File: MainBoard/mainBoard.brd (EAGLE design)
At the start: 99.3 x 99.3 mm, 89 parts, among them IC1 74HC238, IC2 74HC238, IC3 74HC151D, J1 22-05-7038-03, J2 22-05-7038-03, J3 22-05-7038-03, J4 22-05-7038-03, J5 22-05-7038-03, J6 22-05-7038-03, J7 22-05-7038-03, J8 22-05-7038-03, Q1 BC847ASMD, Q10 BC847ASMD, Q2 BC847ASMD, Q5 BC847ASMD, Q6 BC847ASMD, Q9 BC847ASMD, X1 PWR12, X2 MSTBA2, X3 MSTBA2, X4 MSTBA2, X5 MSTBA2, X6 MSTBA2, X7 MSTBA2

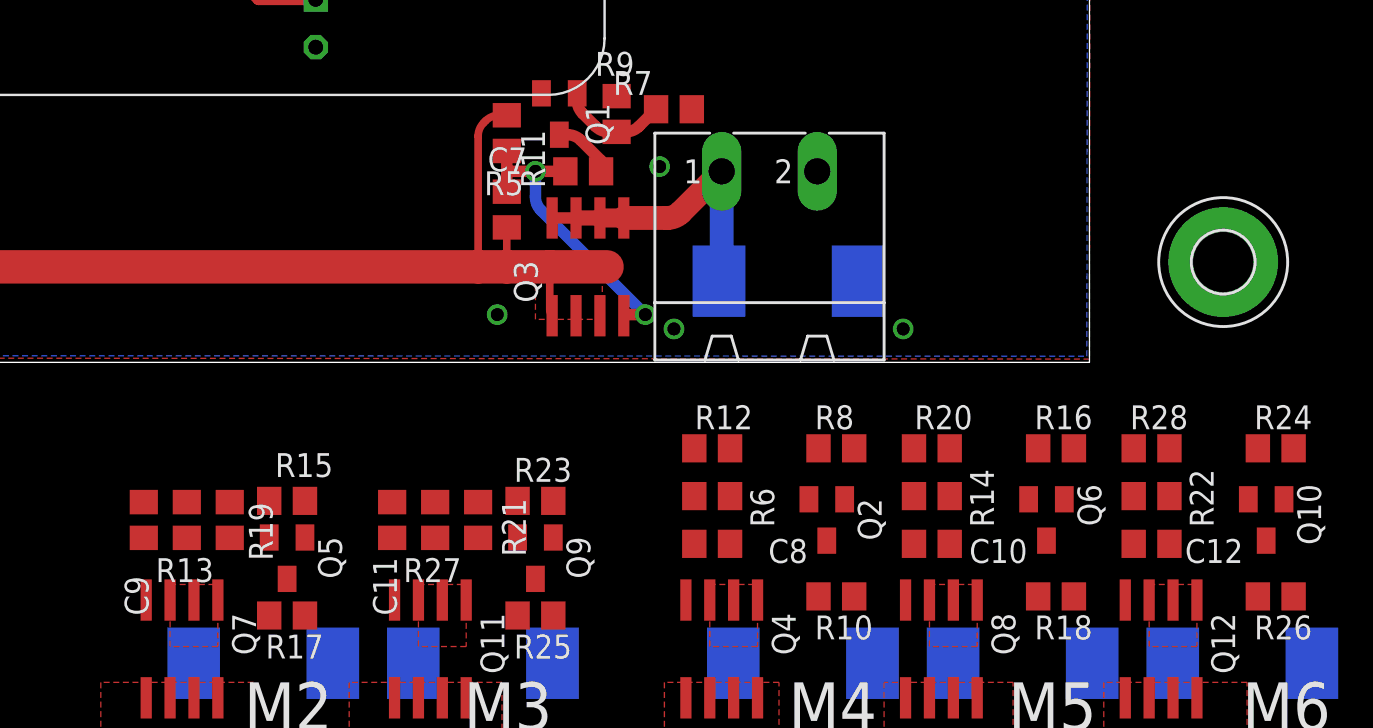
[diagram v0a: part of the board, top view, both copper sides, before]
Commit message: mainboard updates motor curcuit
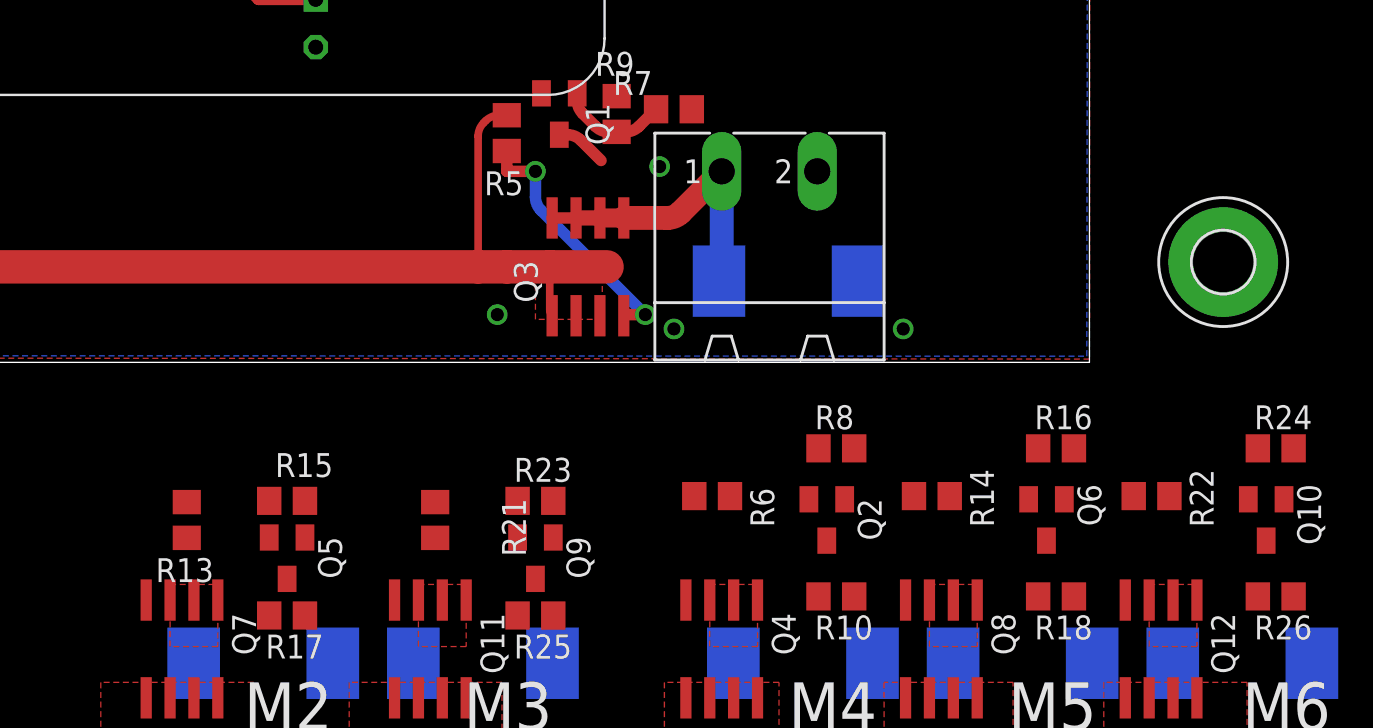
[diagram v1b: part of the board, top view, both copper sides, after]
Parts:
- removed C10, C11, C12, C7, C8, C9: 100n, rcl:C0805
- removed R11, R12, R19, R20, R27, R28: 560, rcl:R0805
- R15, R16, R23, R24, R7, R8: value 10k -> 100
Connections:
- removed net N$10: Q9.3, R27.1
- removed net N$14: Q2.3, R12.1
- removed net N$16: C10.2, Q8.4, R14.1, R20.2
- removed net N$19: C12.2, Q12.4, R22.1, R28.2
- removed net N$4: Q1.3, R11.1
- removed net N$6: Q5.3, R19.1
- net +15V: no longer C10.1, C11.1, C12.1, C7.1, C8.1, C9.1
- net N$13: now also Q2.3; no longer C8.2, R12.2
- net N$17: now also Q8.4, R14.1; no longer R20.1
- net N$2: now also Q5.3; no longer C9.2, R19.2
- net N$21: now also Q12.4, R22.1; no longer R28.1
- net N$3: now also Q1.3; no longer C7.2, R11.2
- net N$8: now also Q9.3; no longer C11.2, R27.2
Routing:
- net N$4: track 3.30 -> 0.00 mm
- net +15V: track 173.4 -> 171.3 mm

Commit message: mainboard updates
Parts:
- removed D5, D7: (no value), diode:SMC
- removed Q10, Q6: BC847ASMD, transistor-npn:SOT23
- removed Q12, Q8: (no value), transistor-power:SO-08
- removed R14, R22: 1k2, rcl:R0805
- removed R16, R24: 100, rcl:R0805
- removed R18, R26: 18k, rcl:R0805
- removed X6, X7: MSTBA2, con-phoenix-508:MSTBA2
- moved Q2 72.9 mm to (14.7, 9.91)
- moved R10 70.5 mm to (17.8, 5.84), turned to 90 degrees
- moved R8 69.6 mm to (17.8, 10.2), turned to 270 degrees
- moved X5 68.2 mm to (25.4, 5.08)
- moved R6 66.5 mm to (14.0, 5.33), flipped to the bottom, turned to 270 degrees
- moved Q4 65.7 mm to (18.0, 7.37), flipped to the bottom, turned to 0 degrees
- moved D3 61.5 mm to (26.4, 5.33)
- moved Q9 41.4 mm to (33.8, 9.91)
- moved X4 39.9 mm to (44.5, 5.08)
- moved R25 38.2 mm to (36.8, 5.84), turned to 90 degrees
- moved R23 37.4 mm to (36.8, 10.2), turned to 270 degrees
- moved Q11 35.4 mm to (37.1, 7.37), flipped to the bottom, turned to 0 degrees
- moved R21 34.4 mm to (33.0, 5.33), flipped to the bottom
- moved X3 33.8 mm to (63.5, 5.08)
- moved D6 30.4 mm to (45.5, 5.33)
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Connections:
- removed net N$17: Q6.3, Q8.4, R14.1
- removed net N$18: Q6.1, R16.2, R18.2
- removed net N$21: Q10.3, Q12.4, R22.1
- removed net N$22: Q10.1, R24.2, R26.2
- removed net WP5: D5.C, Q8.5, Q8.6, Q8.7, Q8.8, X6.1
- removed net WP5C: IC1.12, R16.1
- removed net WP6: D7.C, Q12.5, Q12.6, Q12.7, Q12.8, X7.1
- removed net WP6C: IC1.10, R24.1
- net +15V: no longer Q12.1, Q12.2, Q12.3, Q8.1, Q8.2, Q8.3, R14.2, R22.2
- net GND: no longer D5.A, D7.A, Q10.2, Q6.2, R18.1, R26.1, X6.2, X7.2
- net WP4C: now also IC1.12; no longer IC1.11
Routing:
- net WP4C: track 0.00 -> 75.3 mm
- net WP3C: track 0.00 -> 57.8 mm
- net WP2C: track 0.00 -> 40.4 mm
- net WP1C: track 0.00 -> 22.9 mm
- net +15V: track 171.3 -> 188.5 mm
- net WP1: track 15.9 -> 0.00 mm
- net N$3: track 16.5 -> 6.89 mm, vias 2 -> 1
- net N$8: track 0.00 -> 6.89 mm, vias 0 -> 1
- net N$13: track 0.00 -> 6.89 mm, vias 0 -> 1
- net N$2: track 0.00 -> 6.89 mm, vias 0 -> 1
- net N$15: track 0.00 -> 5.62 mm
- net N$11: track 0.00 -> 5.62 mm
- net N$7: track 0.00 -> 5.58 mm
- added copper zone on layer 16, net +15V
- added copper zone on layer 16, net WP1
- added copper zone on layer 16, net WP2
- added copper zone on layer 16, net WP3
- added copper zone on layer 16, net WP4
- removed copper zone on layer 1, net +15V
- removed copper zone on layer 1, net WP2
- removed copper zone on layer 1, net WP3
- removed copper zone on layer 1, net WP4
- removed copper zone on layer 1, net WP5
- removed copper zone on layer 1, net WP6
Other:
- outline, holes or cut-outs redrawn
- board text removed: "GND [+]"
- board text removed: "M2"
- board text removed: "M3"
- board text removed: "M4"
- board text removed: "M5"
- board text removed: "M6"

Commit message: mainboard updates
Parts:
- removed J6, J7, J8: 22-05-7038-03, con-molex:7395-03
- added D5: (no value), diode:DO-214AC
- added Q6: BC847ASMD, transistor-npn:SOT23
- added Q8: (no value), transistor-power:SO-08
- added R11: 100, rcl:R0805
- added R12: 18k, rcl:R0805
- added R14: 1k2, rcl:R0805
- added X6: MSTBA2, con-phoenix-508:MSTBA2
- D2, D3, D4, D6: device diode:SMC -> diode:DO-214AC
- moved D6 51.3 mm to (94.0, 22.1), turned to 90 degrees
- moved D3 37.1 mm to (63.5, 5.59)
- moved R4 33.6 mm to (111.3, 31.2)
- moved D4 20.1 mm to (44.5, 5.59)
- moved IC3 12.4 mm to (83.6, 55.9), turned to 90 degrees
- moved IC2 12.2 mm to (83.6, 68.3)
- moved J1 8.39 mm to (94.0, 77.5)
- moved J2 8.39 mm to (94.0, 69.3)
- moved J3 8.39 mm to (94.0, 61.2)
- moved J4 8.39 mm to (94.0, 53.1)
- moved J5 8.39 mm to (94.0, 45.0)
- moved IC1 2.84 mm to (85.6, 32.8)
- moved U$2 2.54 mm to (35.3, 75.9)
- moved D2 1.05 mm to (82.5, 5.59)
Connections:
- removed net S6_3V: IC2.10, J6.1
- removed net S6_DAT: IC3.14, J6.2
- removed net S7_3V: IC2.9, J7.1
- removed net S7_DAT: IC3.13, J7.2
- removed net S8_3V: IC2.7, J8.1
- removed net S8_DAT: IC3.12, J8.2
- new net N$4: Q6.3, Q8.4, R14.1
- new net N$6: Q6.1, R11.2, R12.2
- new net WP5: D6.C, Q8.5, Q8.6, Q8.7, Q8.8, X6.1
- new net WP5C: IC1.11, R11.1
- net +15V: now also Q8.1, Q8.2, Q8.3, R14.2
- net GND: now also D5.A, Q6.2, R12.1, X6.2; no longer J6.3, J7.3, J8.3
- net WP2: now also D3.C; no longer D4.C
- net WP3: now also D4.C; no longer D6.C
- net WP4: now also D5.C; no longer D3.C
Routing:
- net +15V: track 188.5 -> 208.3 mm
- net N$4: track 0.00 -> 15.9 mm, vias 0 -> 1
- net WP5C: track 0.00 -> 13.1 mm, vias 0 -> 2
- net N$6: track 0.00 -> 11.1 mm
- net WP4C: track 75.3 -> 78.8 mm
- net WP3C: track 57.8 -> 61.0 mm
- net WP2C: track 40.4 -> 43.2 mm
- net WP1C: track 22.9 -> 25.5 mm
- net +5V: track 127.0 -> 125.6 mm
- net SPI1_MOSI: track 18.6 -> 19.8 mm
- net SPI1_SCK: track 25.1 -> 26.2 mm
- net LED_ERR: track 34.0 -> 35.0 mm
- net SPI1_MISO: track 11.7 -> 12.7 mm
- net STM_TXD: track 48.5 -> 47.4 mm
- net STM_RXD: track 54.0 -> 53.0 mm
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- added copper zone on layer 16, net WP5
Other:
- board text removed: "1"
- board text removed: "2"
- board text removed: "3"
- board text removed: "4"
- board text removed: "7"
- board text removed: "8"
- board text removed: "S6"
- board text removed: "S7"
- board text removed: "S8"

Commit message: mainboard updates
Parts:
- IC1, IC2: value 74HC238 -> 74HC138D
- moved R4 60.5 mm to (62.0, 66.3), turned to 0 degrees
- moved IC3 2.87 mm to (81.5, 53.8)
- moved IC2 2.27 mm to (81.5, 67.3)
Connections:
- removed net 3V3: U$2.1, U$2.23
- removed net N$24: IC2.4, IC2.5
- removed net VCC: IC1.16
- new net +3V3: IC1.16, IC2.16, IC3.16, U$2.1, U$2.23
- net +5V: no longer IC2.16, IC3.16
- net FREQ: now also U$2.28
- net GND: now also IC2.4, IC2.5
- net SEN_A0: now also U$2.27
- net SEN_A1: now also U$2.26
- net SEN_A2: now also U$2.25
- net SEN_ENABLE: now also U$2.17
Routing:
- net +3V3: track 0.00 -> 145.3 mm, vias 0 -> 3
- net 3V3: track 48.0 -> 0.00 mm, vias 2 -> 0
- net SEN_A0: track 0.00 -> 47.4 mm
- net SEN_ENABLE: track 0.00 -> 43.8 mm, vias 0 -> 2
- net SEN_A2: track 0.00 -> 41.7 mm
- net SEN_A1: track 0.00 -> 40.7 mm
- net FREQ: track 0.00 -> 38.0 mm
- net S1_DAT: track 0.00 -> 30.3 mm
- net S2_DAT: track 0.00 -> 23.5 mm
- net S5_3V: track 0.00 -> 23.0 mm, vias 0 -> 1
- net S5_DAT: track 0.00 -> 18.7 mm, vias 0 -> 1
- net S4_3V: track 0.00 -> 16.7 mm, vias 0 -> 1
- net S3_DAT: track 0.00 -> 16.5 mm
- net S1_3V: track 0.00 -> 14.9 mm
- net S3_3V: track 0.00 -> 11.4 mm, vias 0 -> 1
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
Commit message: board updates
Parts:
- added SJ1, SJ2: (no value), jumper:SJ_2
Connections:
- new net RPI_3V3: PCB1.1, PCB1.17, SJ1.1
- new net RPI_5V: PCB1.2, PCB1.4, SJ2.1
- new net STM_3V3: SJ1.3, U$2.1, U$2.23, U$2.40
- new net STM_5V: SJ2.3, U$2.3
- net +3V3: now also SJ1.2; no longer U$2.1, U$2.23
- net +5V: now also SJ2.2; no longer PCB1.2, PCB1.4, U$2.3
- net GND: now also U$2.10, U$2.11, U$2.12, U$2.13, U$2.16, U$2.18, U$2.19, U$2.20, U$2.32, U$2.33, U$2.34, U$2.5, U$2.6, U$2.7, U$2.8, U$2.9
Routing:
- net +3V3: track 145.3 -> 84.8 mm
- net STM_3V3: track 0.00 -> 51.2 mm
- net +5V: track 125.8 -> 77.6 mm, vias 3 -> 1
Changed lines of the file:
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@@
 <?xml version="1.0" encoding="utf-8"?>
 <!DOCTYPE eagle SYSTEM "eagle.dtd">
-<eagle version="6.5.0">
+<eagle version="6.6.0">
 <drawing>
 <settings>
@@
 <attribute name="NAME" x="86.614" y="16.002" size="1.778" layer="25" ratio="10" rot="R90"/>
 </element>
+<element name="SJ1" library="jumper" package="SJ_2" value="" x="-10.668" y="-3.048"/>
+<element name="SJ2" library="jumper" package="SJ_2" value="" x="-10.668" y="-7.112"/>
 </elements>
 <signals>
@@
 <via x="2.54" y="69.596" extent="1-16" drill="0.7"/>
 <wire x1="2.54" y1="69.596" x2="2.54" y2="71.34" width="0.6096" layer="1"/>
-<contactref element="PCB1" pad="4"/>
-<contactref element="PCB1" pad="2"/>
-<contactref element="U$2" pad="3"/>
-<wire x1="72.263" y1="22.606" x2="72.263" y2="25.146" width="1.016" layer="1"/>
-<wire x1="72.263" y1="25.146" x2="75.438" y2="25.146" width="1.016" layer="1"/>
-<wire x1="75.438" y1="25.146" x2="75.438" y2="24.892" width="1.016" layer="1"/>
-<via x="75.438" y="24.892" extent="1-16" drill="1"/>
-<wire x1="75.438" y1="24.892" x2="75.438" y2="25.146" width="1.016" layer="16"/>
-<wire x1="75.438" y1="25.146" x2="49.6902125" y2="25.146" width="1.016" layer="16"/>
-<wire x1="49.6902125" y1="25.146" x2="48.98310625" y2="25.43889375" width="1.016" layer="16" curve="-45"/>
-<wire x1="48.98310625" y1="25.43889375" x2="44.196" y2="30.226" width="1.016" layer="16"/>
-<via x="44.196" y="30.226" extent="1-16" drill="1"/>
-<wire x1="44.196" y1="30.226" x2="40.894" y2="30.226" width="1.016" layer="1"/>
-<wire x1="40.894" y1="30.226" x2="35.4662125" y2="30.226" width="1.016" layer="1"/>
 <wire x1="35.4662125" y1="30.226" x2="34.75910625" y2="30.51889375" width="1.016" layer="1" curve="-45"/>
 <wire x1="34.75910625" y1="30.51889375" x2="17.56489375" y2="47.71310625" width="1.016" layer="1"/>
@@
 <wire x1="13.716" y1="68.138" x2="14.169871875" y2="68.326" width="0.6096" layer="1" curve="-45"/>
 <wire x1="14.169871875" y1="68.326" x2="17.272" y2="68.326" width="0.6096" layer="1"/>
+<contactref element="SJ2" pad="2"/>
+<wire x1="-10.668" y1="-7.112" x2="34.75910625" y2="30.51889375" width="0" layer="19" extent="1-1"/>
 </signal>
 <signal name="N$9">
@@
 <contactref element="C3" pad="-"/>
 <contactref element="R1" pad="2"/>
-<contactref element="PCB1" pad="34"/>
 <contactref element="PCB1" pad="14"/>
 <contactref element="PCB1" pad="14"/>
-<contactref element="PCB1" pad="34"/>
 <contactref element="JP1" pad="3"/>
 <via x="2.54" y="66.294" extent="1-16" drill="0.7"/>
@@
 <contactref element="U$2" pad="22"/>
 <contactref element="U$2" pad="2"/>
-<contactref element="PCB1" pad="9"/>
-<contactref element="PCB1" pad="9"/>
-<contactref element="PCB1" pad="6"/>
-<contactref element="PCB1" pad="6"/>
-<contactref element="PCB1" pad="20"/>
-<contactref element="PCB1" pad="20"/>
-<contactref element="PCB1" pad="25"/>
-<contactref element="PCB1" pad="25"/>
-<contactref element="PCB1" pad="30"/>
-<contactref element="PCB1" pad="30"/>
 <contactref element="JP2" pad="3"/>
 <via x="9.398" y="70.612" extent="1-16" drill="0.7"/>
@@
 <via x="10.922" y="22.352" extent="1-16" drill="0.7"/>
 <contactref element="PCB1" pad="PE_BR"/>
-<contactref element="PCB1" pad="P$2"/>
 <contactref element="IC1" pad="8"/>
 <contactref element="IC1" pad="4"/>
@@
 <via x="76.2" y="67.564" extent="1-16" drill="0.7"/>
 <via x="76.2" y="73.152" extent="1-16" drill="0.7"/>
+<contactref element="U$2" pad="34"/>
+<contactref element="U$2" pad="33"/>
+<contactref element="U$2" pad="32"/>
+<contactref element="U$2" pad="16"/>
+<contactref element="U$2" pad="13"/>
+<contactref element="U$2" pad="12"/>
+<contactref element="U$2" pad="11"/>
+<contactref element="U$2" pad="10"/>
+<contactref element="U$2" pad="9"/>
+<contactref element="U$2" pad="8"/>
+<contactref element="U$2" pad="7"/>
+<contactref element="U$2" pad="6"/>
+<contactref element="U$2" pad="5"/>
+<contactref element="U$2" pad="20"/>
+<contactref element="U$2" pad="19"/>
+<contactref element="U$2" pad="18"/>
+<contactref element="PCB1" pad="34"/>
+<contactref element="PCB1" pad="20"/>
+<contactref element="PCB1" pad="20"/>
+<contactref element="PCB1" pad="30"/>
+<contactref element="PCB1" pad="30"/>
+<contactref element="PCB1" pad="P$2"/>
+<contactref element="PCB1" pad="25"/>
+<contactref element="PCB1" pad="25"/>
+<contactref element="PCB1" pad="6"/>
+<contactref element="PCB1" pad="6"/>
+<contactref element="PCB1" pad="9"/>
+<contactref element="PCB1" pad="9"/>
 </signal>
 <signal name="N$29">
@@
 <contactref element="IC2" pad="16"/>
 <contactref element="IC1" pad="16"/>
-<contactref element="U$2" pad="1"/>
-<contactref element="U$2" pad="23"/>
 <wire x1="78.4606" y1="49.403" x2="80.645" y2="49.403" width="0.6096" layer="1"/>
 <wire x1="80.645" y1="49.403" x2="80.772" y2="49.53" width="0.6096" layer="1"/>
@@
 <via x="83.058" y="47.244" extent="1-16" drill="0.7"/>
 <wire x1="83.058" y1="47.244" x2="80.772" y2="49.53" width="0.6096" layer="16"/>
-<wire x1="40.894" y1="25.146" x2="44.0357875" y2="25.146" width="0.6096" layer="1"/>
-<wire x1="44.0357875" y1="25.146" x2="44.74289375" y2="25.43889375" width="0.6096" layer="1" curve="45"/>
-<wire x1="44.74289375" y1="25.43889375" x2="47.96710625" y2="28.66310625" width="0.6096" layer="1"/>
-<wire x1="47.96710625" y1="28.66310625" x2="48.26" y2="29.3702125" width="0.6096" layer="1" curve="45"/>
-<wire x1="48.26" y1="29.3702125" x2="48.26" y2="65.8797875" width="0.6096" layer="1"/>
-<wire x1="48.26" y1="65.8797875" x2="48.55289375" y2="66.58689375" width="0.6096" layer="1" curve="-45"/>
-<wire x1="48.55289375" y1="66.58689375" x2="49.99910625" y2="68.03310625" width="0.6096" layer="1"/>
-<wire x1="49.99910625" y1="68.03310625" x2="50.7062125" y2="68.326" width="0.6096" layer="1" curve="-45"/>
-<wire x1="50.7062125" y1="68.326" x2="52.578" y2="68.326" width="0.6096" layer="1"/>
-<wire x1="52.578" y1="68.326" x2="61.8157875" y2="68.326" width="0.6096" layer="1"/>
 <wire x1="61.8157875" y1="68.326" x2="62.52289375" y2="68.61889375" width="0.6096" layer="1" curve="45"/>
 <wire x1="62.52289375" y1="68.61889375" x2="64.98510625" y2="71.08110625" width="0.6096" layer="1"/>
@@
 <wire x1="79.8497875" y1="73.914" x2="80.55689375" y2="73.62110625" width="0.6096" layer="1" curve="-45"/>
 <wire x1="80.55689375" y1="73.62110625" x2="82.042" y2="72.136" width="0.6096" layer="1"/>
+<contactref element="SJ1" pad="2"/>
+<wire x1="-10.668" y1="-3.048" x2="61.8157875" y2="68.326" width="0" layer="19" extent="1-1"/>
+</signal>
+<signal name="STM_3V3">
+<contactref element="U$2" pad="1"/>
+<contactref element="U$2" pad="23"/>
+<contactref element="U$2" pad="40"/>
+<wire x1="40.894" y1="25.146" x2="44.0357875" y2="25.146" width="0.6096" layer="1"/>
+<wire x1="44.0357875" y1="25.146" x2="44.74289375" y2="25.43889375" width="0.6096" layer="1" curve="45"/>
+<wire x1="44.74289375" y1="25.43889375" x2="47.96710625" y2="28.66310625" width="0.6096" layer="1"/>
+<wire x1="47.96710625" y1="28.66310625" x2="48.26" y2="29.3702125" width="0.6096" layer="1" curve="45"/>
+<wire x1="48.26" y1="29.3702125" x2="48.26" y2="65.8797875" width="0.6096" layer="1"/>
+<wire x1="48.26" y1="65.8797875" x2="48.55289375" y2="66.58689375" width="0.6096" layer="1" curve="-45"/>
+<wire x1="48.55289375" y1="66.58689375" x2="49.99910625" y2="68.03310625" width="0.6096" layer="1"/>
+<wire x1="49.99910625" y1="68.03310625" x2="50.7062125" y2="68.326" width="0.6096" layer="1" curve="-45"/>
+<wire x1="50.7062125" y1="68.326" x2="52.578" y2="68.326" width="0.6096" layer="1"/>
+<contactref element="SJ1" pad="3"/>
+<wire x1="47.96710625" y1="28.66310625" x2="56.134" y2="25.146" width="0" layer="19" extent="1-1"/>
+<wire x1="-9.144" y1="-3.048" x2="40.894" y2="25.146" width="0" layer="19" extent="1-1"/>
+</signal>
+<signal name="RPI_3V3">
+<contactref element="PCB1" pad="1"/>
+<contactref element="PCB1" pad="17"/>
+<contactref element="SJ1" pad="1"/>
+<wire x1="67.818" y1="22.606" x2="67.818" y2="42.926" width="0" layer="19" extent="1-1"/>
+<wire x1="-12.192" y1="-3.048" x2="67.818" y2="22.606" width="0" layer="19" extent="1-1"/>
+</signal>
+<signal name="RPI_5V">
+<contactref element="PCB1" pad="4"/>
+<contactref element="PCB1" pad="2"/>
+<contactref element="SJ2" pad="1"/>
+<wire x1="72.263" y1="22.606" x2="72.263" y2="25.146" width="0" layer="19" extent="1-1"/>
+<wire x1="-12.192" y1="-7.112" x2="72.263" y2="22.606" width="0" layer="19" extent="1-1"/>
+</signal>
+<signal name="STM_5V">
+<contactref element="U$2" pad="3"/>
+<contactref element="SJ2" pad="3"/>
+<wire x1="-9.144" y1="-7.112" x2="40.894" y2="30.226" width="0" layer="19" extent="1-1"/>
 </signal>
 </signals>

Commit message: mainboard update + gerber export
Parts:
- SJ1: value (none) -> 3V3
- SJ2: value (none) -> 5V
- moved SJ1 86.1 mm to (62.0, 43.2), turned to 180 degrees
- moved SJ2 56.3 mm to (33.5, 27.7), turned to 90 degrees
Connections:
- removed net N$30: PCB1.39
- net GND: now also IC3.12, IC3.13, IC3.14, PCB1.39
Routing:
- net RPI_5V: track 0.00 -> 44.1 mm
- net STM_3V3: track 51.2 -> 80.8 mm, vias 0 -> 2
- net RPI_3V3: track 0.00 -> 27.8 mm, vias 0 -> 2
- net STM_5V: track 0.00 -> 7.72 mm
- net +3V3: track 84.8 -> 78.0 mm
- net RPI_NRST: track 10.6 -> 16.6 mm, vias 0 -> 1
- net +5V: track 77.6 -> 79.7 mm
- net SEN_ENABLE: vias 2 -> 0
- net GND: vias 130 -> 138
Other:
- board text added: "RPI"
- board text added: "STM"
- board text removed: "3V3"
- board text removed: "SEN"
